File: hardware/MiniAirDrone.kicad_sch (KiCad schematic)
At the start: 29 parts, among them J1 USB_C_Receptacle_USB2.0, Q1 UMH3N, U1 CH340C, U2 ESP32-WROOM-32, U3 MPU-6050, U4 MS5611-01BA, U5 VL53L1CXV0FY1, U6 TS1117BCW33_RPG

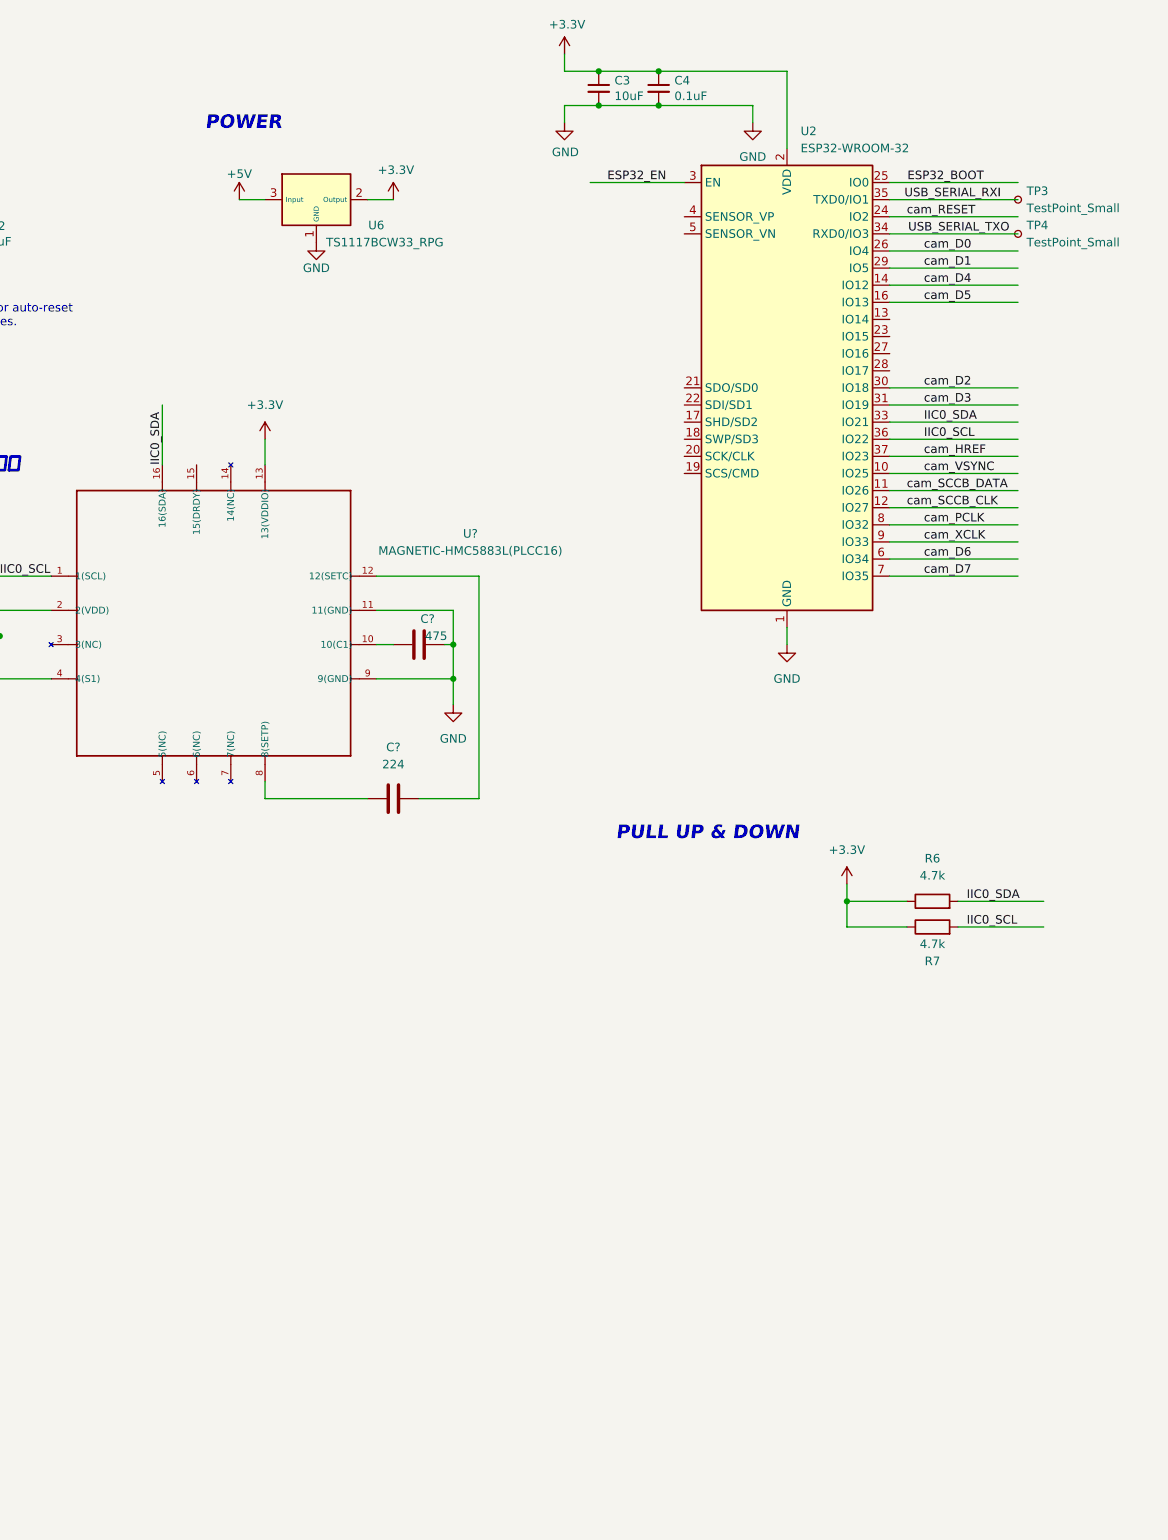
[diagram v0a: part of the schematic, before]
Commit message: cam conn finished
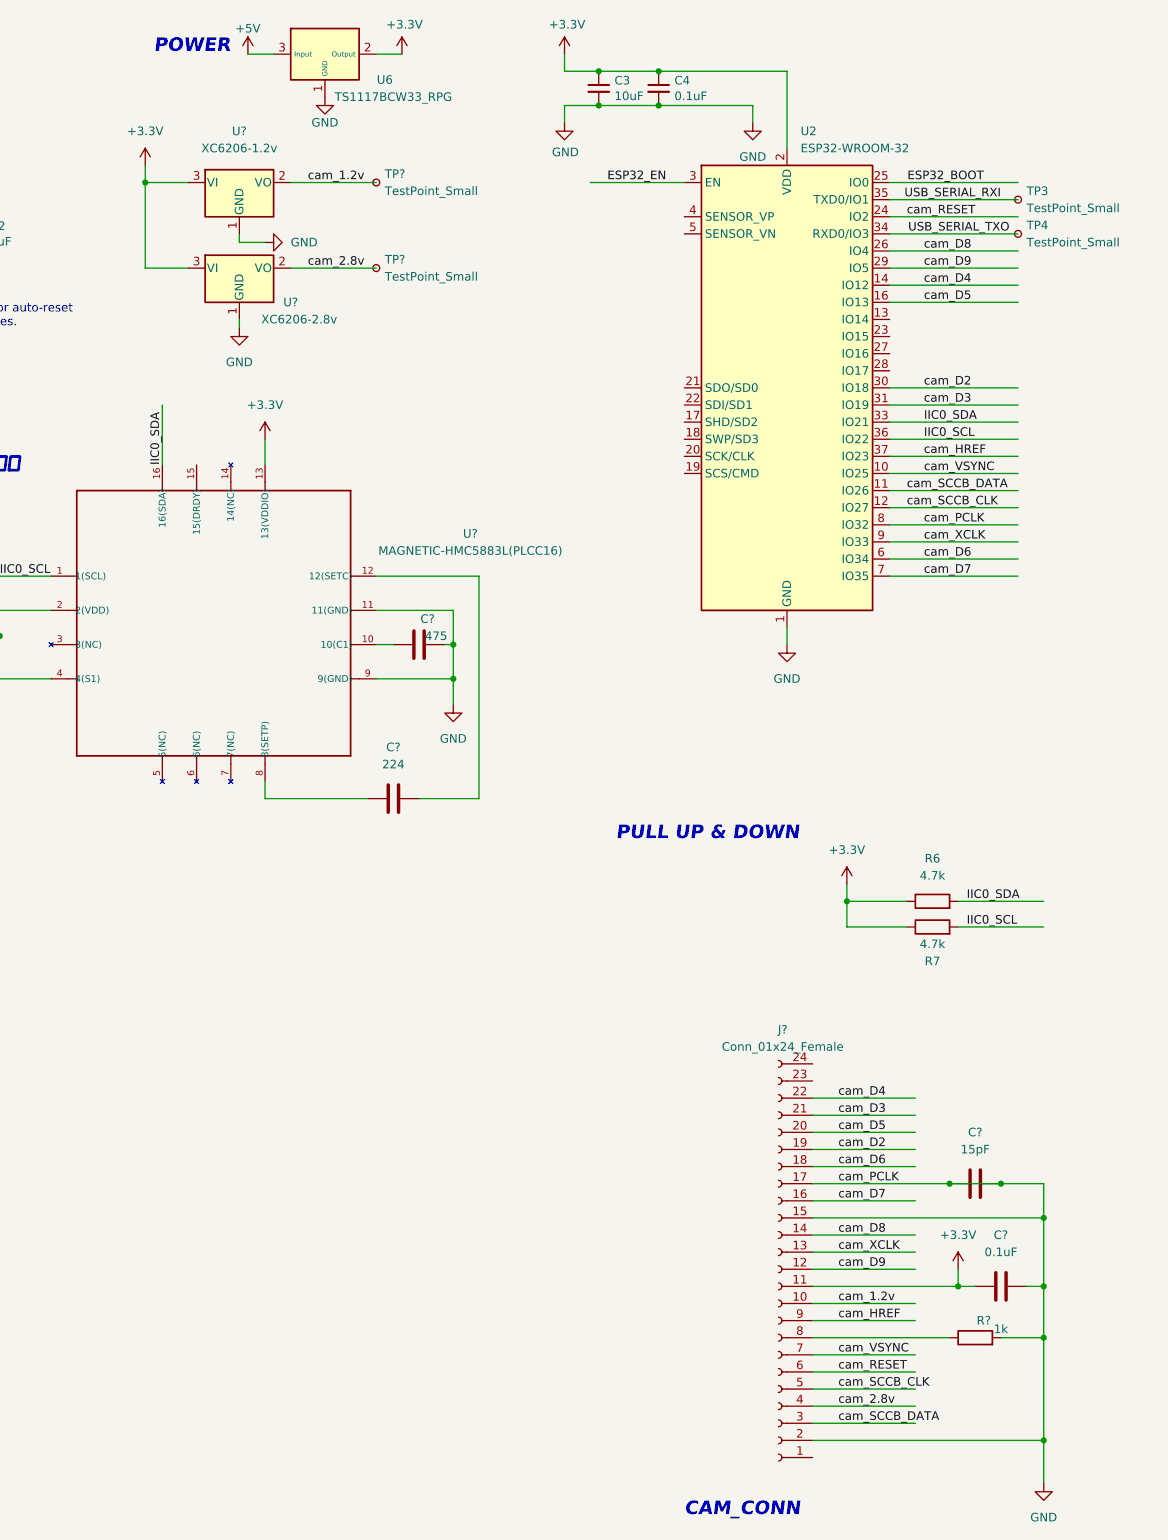
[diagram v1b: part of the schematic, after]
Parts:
- added C?: 0.1uF, symbol Device:C
- added C?: 15pF, symbol Device:C
- added J?: Conn_01x24_Female, symbol Connector:Conn_01x24_Female
- added R?: 1k, symbol Device:R
- added TP? (x2): TestPoint_Small, symbol Connector:TestPoint_Small
- added U?: XC6206-2.8v, Package_TO_SOT_SMD:SOT-23, symbol Regulator_Linear:XC6206PxxxMR
- added U?: XC6206-1.2v, Package_TO_SOT_SMD:SOT-23, symbol Regulator_Linear:XC6206PxxxMR
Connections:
- net cam_PCLK is gone; now on net GND: U2.8 (IO32)
- net +3.3V: now also C?.1, J?.11 (Pin_11), U?.3 (VI), U?.3 (VI)
- net GND: now also C?.1, C?.2, C?.2, J?.15 (Pin_15), J?.17 (Pin_17), J?.2 (Pin_2), R?.2, U?.1 (GND), U?.1 (GND)
- net cam_D2: now also J?.19 (Pin_19)
- net cam_D3: now also J?.21 (Pin_21)
- net cam_D4: now also J?.22 (Pin_22)
- net cam_D5: now also J?.20 (Pin_20)
- net cam_D6: now also J?.18 (Pin_18)
- net cam_D7: now also J?.16 (Pin_16)
- net cam_HREF: now also J?.9 (Pin_9)
- net cam_RESET: now also J?.6 (Pin_6)
- net cam_SCCB_CLK: now also J?.5 (Pin_5)
- net cam_SCCB_DATA: now also J?.3 (Pin_3)
- net cam_VSYNC: now also J?.7 (Pin_7)
- net cam_XCLK: now also J?.13 (Pin_13)
- net cam_D0 renamed cam_D8
- net cam_D8: now also J?.14 (Pin_14)
- net cam_D1 renamed cam_D9
- net cam_D9: now also J?.12 (Pin_12)
- new net: J?.8 (Pin_8), R?.1
- new net cam_1.2v: J?.10 (Pin_10), TP?.1, U?.2 (VO)
- new net cam_2.8v: J?.4 (Pin_4), TP?.1, U?.2 (VO)
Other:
- note added: "CAM_CONN"
- moved on the sheet: U6

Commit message: sth
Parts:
- added J?: Bus_PCI_Express_Mini, symbol Connector:Bus_PCI_Express_Mini
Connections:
- new net: J?.15 (GND), J?.18 (GND), J?.21 (GND), J?.26 (GND), J?.27 (GND), J?.29 (GND), J?.34 (GND), J?.35 (GND), J?.37 (GND), J?.4 (GND), J?.40 (GND), J?.43 (GND), J?.50 (GND), J?.9 (GND)
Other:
- note added: "LTE EC20"
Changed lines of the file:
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@@
+    (effects (font (size 2.0066 2.0066) (thickness 0.4013) bold italic) (justify left bottom))
+  )
+  (text "LTE EC20" (at 252.73 156.21 0)
     (effects (font (size 2.0066 2.0066) (thickness 0.4013) bold italic) (justify left bottom))
   )
@@
     (pin "1")
   )
+  (symbol (lib_id "Connector:Bus_PCI_Express_Mini") (at 292.1 196.85 0) (unit 1)
+    (in_bom yes) (on_board yes) (fields_autoplaced)
+    (property "Reference" "J?" (id 0) (at 296.6594 227.33 0)
+      (effects (font (size 1.27 1.27)) (justify left))
+    )
+    (property "Value" "Bus_PCI_Express_Mini" (id 1) (at 296.6594 229.87 0)
+      (effects (font (size 1.27 1.27)) (justify left))
+    )
+    (property "Footprint" "" (id 2) (at 292.1 196.85 0)
+      (effects (font (size 1.27 1.27)) hide)
+    )
+    (property "Datasheet" "~" (id 3) (at 288.29 226.06 0)
+      (effects (font (size 1.27 1.27)) hide)
+    )
+    (pin "1")
+    (pin "10")
+    (pin "11")
+    (pin "12")
+    (pin "13")
+    (pin "14")
+    (pin "15")
+    (pin "16")
+    (pin "17")
+    (pin "18")
+    (pin "19")
+    (pin "2")
+    (pin "20")
+    (pin "21")
+    (pin "22")
+    (pin "23")
+    (pin "24")
+    (pin "25")
+    (pin "26")
+    (pin "27")
+    (pin "28")
+    (pin "29")
+    (pin "3")
+    (pin "30")
+    (pin "31")
+    (pin "32")
+    (pin "33")
+    (pin "34")
+    (pin "35")
+    (pin "36")
+    (pin "37")
+    (pin "38")
+    (pin "39")
+    (pin "4")
+    (pin "40")
+    (pin "41")
+    (pin "42")
+    (pin "43")
+    (pin "44")
+    (pin "45")
+    (pin "46")
+    (pin "47")
+    (pin "48")
+    (pin "49")
+    (pin "5")
+    (pin "50")
+    (pin "51")
+    (pin "52")
+    (pin "6")
+    (pin "7")
+    (pin "8")
+    (pin "9")
+    (pin "MP")
+  )
   (symbol (lib_id "power:+3.3V") (at 191.77 86.36 0) (unit 1)
     (in_bom yes) (on_board yes) (fields_autoplaced)
@@
       (reference "J?") (unit 1) (value "Conn_01x24_Female") (footprint "")
     )
+    (path "/d4a18e38-69e6-43e0-b7b2-6ac7c773e85d"
+      (reference "J?") (unit 1) (value "Bus_PCI_Express_Mini") (footprint "")
+    )
     (path "/dd9dc849-7525-4046-8ee2-5503b52cf2a3"
